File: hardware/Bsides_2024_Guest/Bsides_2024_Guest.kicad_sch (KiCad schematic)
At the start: 44 parts, among them J1 Add_On, J2 Battery, J3 Battery, J4 OLED, J5 Conn_01x05, J6 Conn_01x05, P1 USB_C_Plug_USB2.0, Q1 DMG3415U-7, SW1 ON, SW2 RESET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

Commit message: feat(Hw): Update schematics
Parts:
- J4: manf# I2C SH1106 Display Oled Azul 128×64 1.3 ” -> Display OLED 128×32 0.91 I2C SSD1306 Blanco / Azul
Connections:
- net GND: now also J4.4 (Pin_4); no longer J4.2 (Pin_2)
- net SCL: now also J4.2 (Pin_2); no longer J4.3 (Pin_3)
- net SDA: now also J4.1 (Pin_1); no longer J4.4 (Pin_4)
- net VOUT: now also J4.3 (Pin_3); no longer J4.1 (Pin_1)
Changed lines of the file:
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@@
 	(wire
 		(pts
-			(xy 76.2 118.11) (xy 82.55 118.11)
-		)
-		(stroke
-			(width 0)
-			(type default)
-		)
-	)
-	(wire
-		(pts
 			(xy 192.024 119.761) (xy 196.215 119.761)
 		)
@@
 	(wire
 		(pts
-			(xy 76.2 120.65) (xy 82.55 120.65)
-		)
-		(stroke
-			(width 0)
-			(type default)
-		)
-	)
-	(wire
-		(pts
 			(xy 199.136 69.85) (xy 199.136 70.358)
 		)
@@
 	(wire
 		(pts
+			(xy 80.01 116.84) (xy 77.47 116.84)
+		)
+		(stroke
+			(width 0)
+			(type default)
+		)
+	)
+	(wire
+		(pts
 			(xy 58.674 79.756) (xy 62.484 79.756)
 		)
@@
 	(wire
 		(pts
-			(xy 76.2 123.19) (xy 82.55 123.19)
-		)
-		(stroke
-			(width 0)
-			(type default)
-		)
-	)
-	(wire
-		(pts
 			(xy 58.674 37.846) (xy 70.612 37.846)
 		)
@@
 	(wire
 		(pts
+			(xy 80.01 119.38) (xy 77.47 119.38)
+		)
+		(stroke
+			(width 0)
+			(type default)
+		)
+	)
+	(wire
+		(pts
 			(xy 262.89 119.761) (xy 266.7 119.761)
 		)
@@
 	(wire
 		(pts
-			(xy 76.2 115.57) (xy 82.55 115.57)
-		)
-		(stroke
-			(width 0)
-			(type default)
-		)
-	)
-	(wire
-		(pts
 			(xy 26.67 116.84) (xy 29.21 116.84)
 		)
@@
 	(wire
 		(pts
+			(xy 80.01 121.92) (xy 77.47 121.92)
+		)
+		(stroke
+			(width 0)
+			(type default)
+		)
+	)
+	(wire
+		(pts
 			(xy 251.587 89.154) (xy 251.587 85.598)
 		)
@@
 	(wire
 		(pts
+			(xy 80.01 124.46) (xy 77.47 124.46)
+		)
+		(stroke
+			(width 0)
+			(type default)
+		)
+	)
+	(wire
+		(pts
 			(xy 237.49 119.761) (xy 241.808 119.761)
 		)
@@
 		)
 	)
-	(label "SDA"
-		(at 76.2 123.19 0)
-		(fields_autoplaced yes)
-		(effects
-			(font
-				(size 1.27 1.27)
-			)
-			(justify left bottom)
-		)
-	)
 	(label "VOUT"
 		(at 213.36 118.11 0)
@@
 		)
 	)
-	(label "SCL"
-		(at 76.2 120.65 0)
-		(fields_autoplaced yes)
-		(effects
-			(font
-				(size 1.27 1.27)
-			)
-			(justify left bottom)
-		)
-	)
 	(label "PIN"
 		(at 172.466 131.826 0)
@@
 		)
 	)
-	(label "GND"
-		(at 76.2 118.11 0)
+	(label "D+"
+		(at 149.606 59.69 0)
 		(fields_autoplaced yes)
 		(effects
@@
 		)
 	)
-	(label "D+"
-		(at 149.606 59.69 0)
+	(label "D-"
+		(at 29.972 65.786 0)
 		(fields_autoplaced yes)
 		(effects
@@
 		)
 	)
-	(label "D-"
-		(at 29.972 65.786 0)
+	(label "SCL"
+		(at 77.47 119.38 180)
 		(fields_autoplaced yes)
 		(effects
@@
 				(size 1.27 1.27)
 			)
-			(justify left bottom)
+			(justify right bottom)
 		)
 	)
@@
 		)
 	)
+	(label "GND"
+		(at 77.47 124.46 180)
+		(fields_autoplaced yes)
+		(effects
+			(font
+				(size 1.27 1.27)
+			)
+			(justify right bottom)
+		)
+	)
 	(label "BOOT"
 		(at 182.753 67.818 180)
@@
 		)
 	)
-	(label "VOUT"
-		(at 76.2 115.57 0)
-		(fields_autoplaced yes)
-		(effects
-			(font
-				(size 1.27 1.27)
-			)
-			(justify left bottom)
-		)
-	)
 	(label "GPIO15"
 		(at 62.484 71.374 0)
@@
 		)
 	)
+	(label "SDA"
+		(at 77.47 116.84 180)
+		(fields_autoplaced yes)
+		(effects
+			(font
+				(size 1.27 1.27)
+			)
+			(justify right bottom)
+		)
+	)
 	(label "VOUT"
 		(at 85.09 58.42 0)
@@
 		)
 	)
+	(label "VOUT"
+		(at 77.47 121.92 180)
+		(fields_autoplaced yes)
+		(effects
+			(font
+				(size 1.27 1.27)
+			)
+			(justify right bottom)
+		)
+	)
 	(label "BOOT"
 		(at 24.638 71.374 0)
@@
 	)
 	(symbol
+		(lib_id "Connector:Screw_Terminal_01x04")
+		(at 85.09 119.38 0)
+		(unit 1)
+		(exclude_from_sim no)
+		(in_bom yes)
+		(on_board yes)
+		(dnp no)
+		(fields_autoplaced yes)
+		(property "Reference" "J4"
+			(at 87.376 119.3799 0)
+			(effects
+				(font
+					(size 1.27 1.27)
+				)
+				(justify left)
+			)
+		)
+		(property "Value" "OLED"
+			(at 87.376 121.9199 0)
+			(effects
+				(font
+					(size 1.27 1.27)
+				)
+				(justify left)
+			)
+		)
+		(property "Footprint" "bsides:Display OLED 128 x32"
+			(at 85.09 119.38 0)
+			(effects
+				(font
+					(size 1.27 1.27)
+				)
+				(hide yes)
+			)
+		)
+		(property "Datasheet" ""
+			(at 85.09 119.38 0)
+			(effects
+				(font
+					(size 1.27 1.27)
+				)
+				(hide yes)
+			)
+		)
+		(property "Description" ""
+			(at 85.09 119.38 0)
+			(effects
+				(font
+					(size 1.27 1.27)
+				)
+				(hide yes)
+			)
+		)
+		(property "manf#" "Display OLED 128×32 0.91 I2C SSD1306 Blanco / Azul"
+			(at 85.09 119.38 0)
+			(effects
+				(font
+					(size 1.27 1.27)
+				)
+				(hide yes)
+			)
+		)
+		(property "provedor" "UNIT Electronics"
+			(at 85.09 119.38 0)
+			(effects
+				(font
+					(size 1.27 1.27)
+				)
+				(hide yes)
+			)
+		)
+		(pin "1"
+		)
+		(pin "2"
+		)
+		(pin "3"
+		)
+		(pin "4"
+		)
+		(instances
+			(project "Bsides_2024_Guest"
+				(path "/21a57a81-777f-4f81-b806-a7171bf6ef6c"
+					(reference "J4")
+					(unit 1)
+				)
+			)
+		)
+	)
+	(symbol
 		(lib_id "power:GND")
 		(at 199.39 55.88 0)
@@
 					(unit 1)
 				)
-			)
-		)
-	)
-	(symbol
-		(lib_id "Connector:Screw_Terminal_01x04")
-		(at 87.63 118.11 0)
-		(unit 1)
-		(exclude_from_sim no)
-		(in_bom yes)
-		(on_board yes)
-		(dnp no)
-		(fields_autoplaced yes)
-		(property "Reference" "J4"
-			(at 89.916 118.1099 0)
-			(effects
-				(font
-					(size 1.27 1.27)
-				)
-				(justify left)
-			)
-		)
-		(property "Value" "OLED"
-			(at 89.916 120.6499 0)
-			(effects
-				(font
-					(size 1.27 1.27)
-				)
-				(justify left)
-			)
-		)
-		(property "Footprint" "bsides:Display OLED 128 x32"
-			(at 87.63 118.11 0)
-			(effects
-				(font
-					(size 1.27 1.27)
-				)
-				(hide yes)
-			)
-		)
-		(property "Datasheet" "~"
-			(at 87.63 118.11 0)
-			(effects
-				(font
-					(size 1.27 1.27)
-				)
-				(hide yes)
-			)
-		)
-		(property "Description" ""
-			(at 87.63 118.11 0)
-			(effects
-				(font
-					(size 1.27 1.27)
-				)
-				(hide yes)
-			)
-		)
-		(property "manf#" "I2C SH1106 Display Oled Azul 128×64 1.3 ” "
-			(at 87.63 118.11 0)
-			(effects
-				(font
-					(size 1.27 1.27)
-				)
-				(hide yes)
-			)
-		)
-		(property "provedor" "UNIT Electronics"
-			(at 87.63 118.11 0)
-			(effects
-				(font
-					(size 1.27 1.27)
-				)
-				(hide yes)
-			)
-		)
-		(pin "1"
-		)
-		(pin "2"
-		)
-		(pin "3"
-		)
-		(pin "4"
-		)
-		(instances
-			(project "Bsides_2024_Guest"
-				(path "/21a57a81-777f-4f81-b806-a7171bf6ef6c"
-					(reference "J4")
-					(unit 1)
-				)

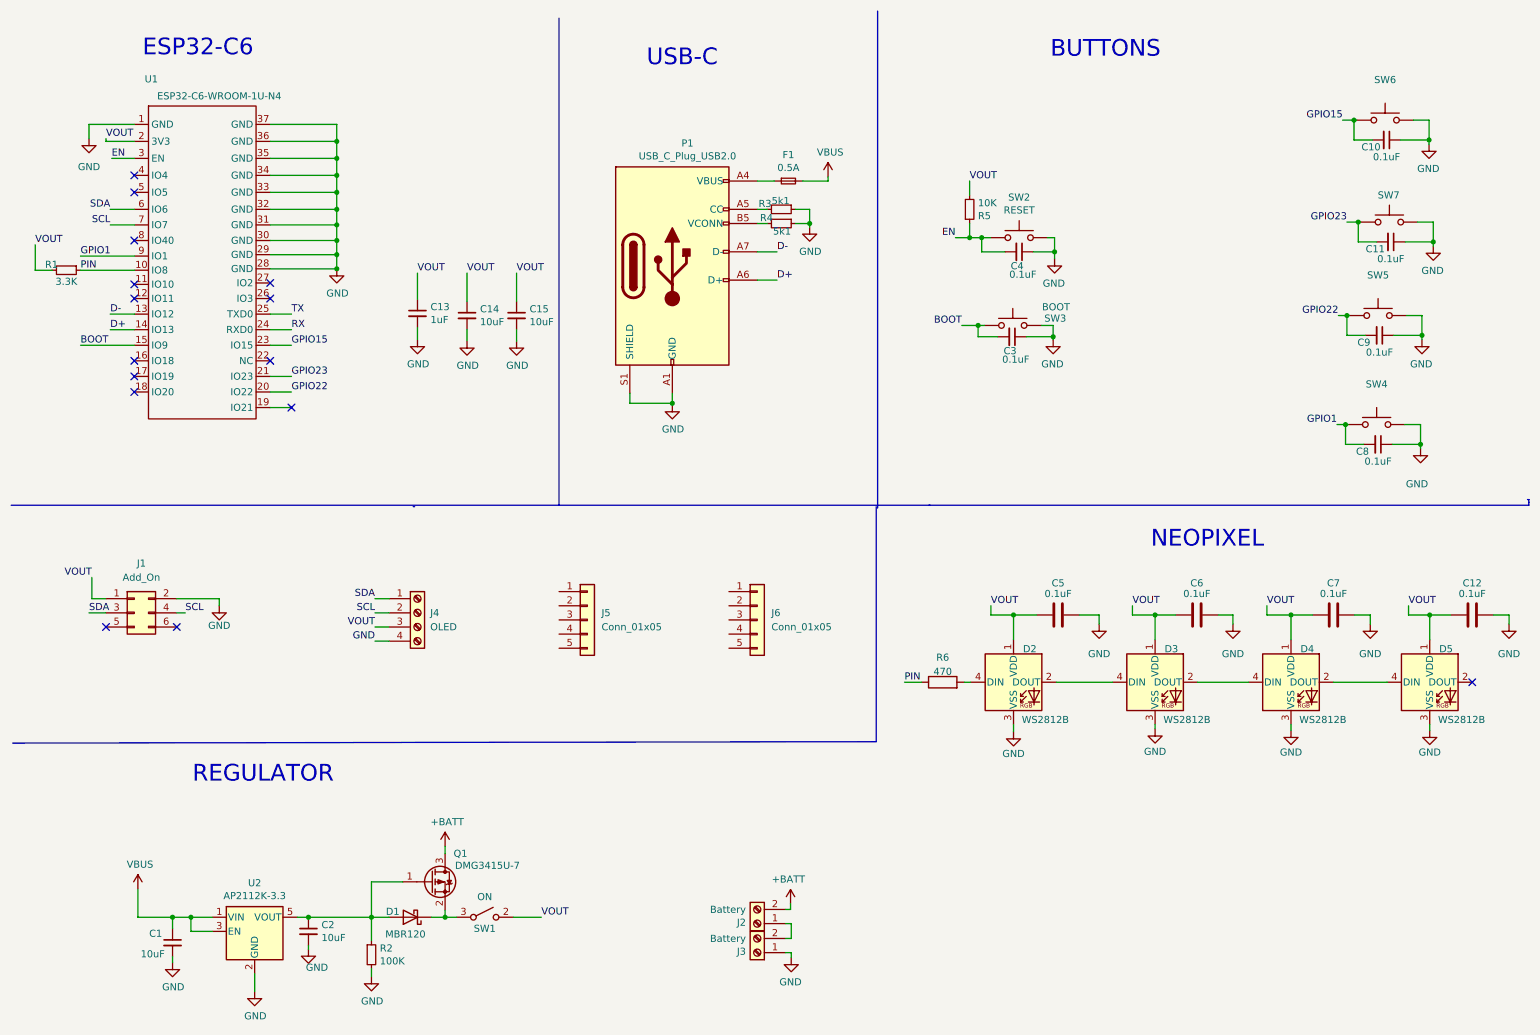
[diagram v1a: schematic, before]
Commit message: feat(Hw): Update route
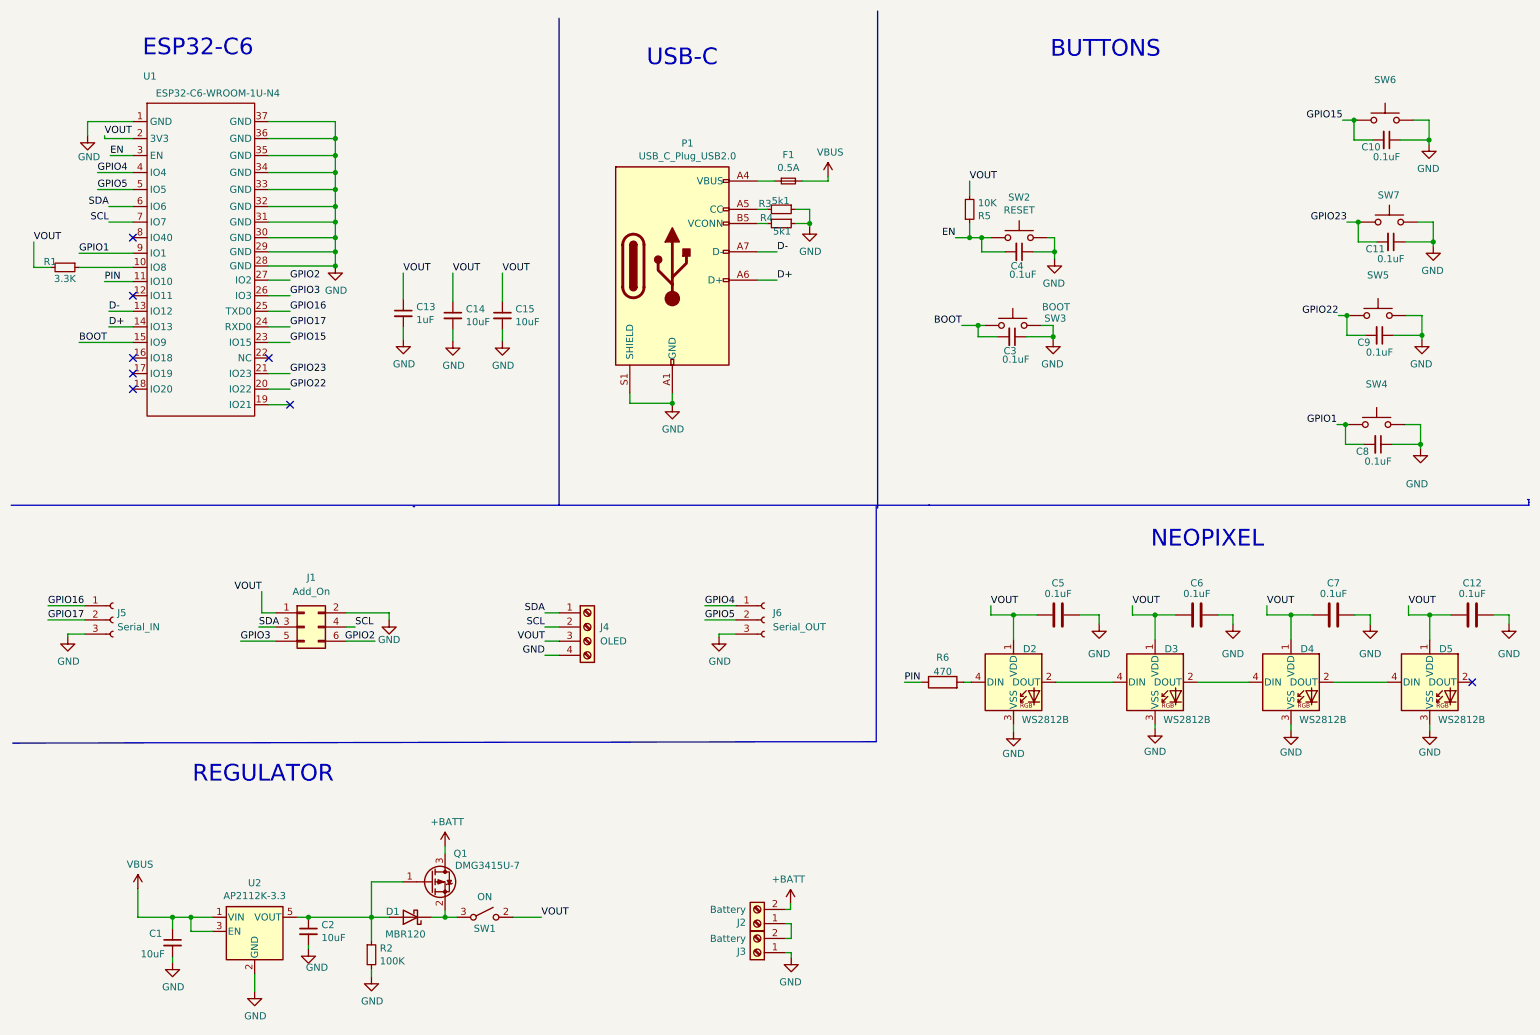
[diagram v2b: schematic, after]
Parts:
- removed J5, J6: Conn_01x05, Connector_PinHeader_2.54mm:PinHeader_1x05_P2.54mm_Vertical, symbol Connector_Generic:Conn_01x05
- added J5: Serial_IN, Connector_PinHeader_2.54mm:PinHeader_1x03_P2.54mm_Vertical, symbol Connector:Conn_01x03_Socket
- added J6: Serial_OUT, Connector_PinSocket_2.54mm:PinSocket_1x03_P2.54mm_Vertical, symbol Connector:Conn_01x03_Socket
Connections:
- net GND: now also J5.3 (Pin_3), J6.3 (Pin_3)
- net PIN: now also U1.11 (IO10); no longer R1.1, U1.10 (IO8)
- net GPIO3: now reaches U1.26 (IO3)
- net GPIO3: now also J1.5 (Pin_5)
- net GPIO2: now reaches U1.27 (IO2)
- net GPIO2: now also J1.6 (Pin_6)
- net GPIO4: now reaches U1.4 (IO4)
- net GPIO4: now also J6.1 (Pin_1)
- net GPIO5: now reaches U1.5 (IO5)
- net GPIO5: now also J6.2 (Pin_2)
- net RX renamed GPIO17
- net GPIO17: now also J5.2 (Pin_2)
- net TX renamed GPIO16
- net GPIO16: now also J5.1 (Pin_1)
- new net: R1.1, U1.10 (IO8)
- no-connect marks 15 -> 8
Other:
- moved on the sheet: C13, C14, C15, J1, J4, R1, U1

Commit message: Update route and schematic
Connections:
- net GPIO1 renamed LEFT
- net LEFT: now also SW7.2; no longer SW4.2
- net GPIO15 renamed RIGHT
- net GPIO22 renamed UP
- net UP: now also SW4.2; no longer SW5.2
- net GPIO23 renamed DOWN
- net DOWN: now also SW5.2; no longer SW7.2
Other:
- moved on the sheet: C8, C9, SW4, SW5, SW7

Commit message: Feat(Hw): Update PCB
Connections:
- net DOWN: now also C9.2; no longer C11.2
- net LEFT: now also C10.2, SW6.2; no longer C8.2, SW7.2
- net RIGHT: now also C11.2, SW7.2; no longer C10.2, SW6.2
- net UP: now also C8.2; no longer C9.2
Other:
- moved on the sheet: C10, SW4, SW5, SW6, SW7
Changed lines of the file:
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@@
 	)
 	(junction
-		(at 266.573 34.544)
+		(at 266.954 32.766)
 		(diameter 0)
 		(color 0 0 0 0)
@@
 	)
 	(junction
-		(at 253.111 30.988)
+		(at 253.492 29.21)
 		(diameter 0)
 		(color 0 0 0 0)
@@
 	(wire
 		(pts
-			(xy 252.222 85.09) (xy 250.698 85.09)
-		)
-		(stroke
-			(width 0)
-			(type default)
-		)
-	)
-	(wire
-		(pts
 			(xy 175.514 131.826) (xy 172.466 131.826)
 		)
@@
 	(wire
 		(pts
-			(xy 266.573 34.544) (xy 266.573 35.306)
+			(xy 266.954 32.766) (xy 266.954 33.528)
 		)
 		(stroke
@@
 	(wire
 		(pts
-			(xy 266.573 34.544) (xy 261.493 34.544)
+			(xy 266.954 32.766) (xy 261.874 32.766)
 		)
 		(stroke
@@
 	(wire
 		(pts
-			(xy 266.573 30.988) (xy 266.573 34.544)
+			(xy 266.954 29.21) (xy 266.954 32.766)
 		)
 		(stroke
@@
 	(wire
 		(pts
-			(xy 256.413 34.544) (xy 253.111 34.544)
+			(xy 256.794 32.766) (xy 253.492 32.766)
 		)
 		(stroke
@@
 	(wire
 		(pts
-			(xy 253.111 34.544) (xy 253.111 30.988)
+			(xy 253.492 32.766) (xy 253.492 29.21)
 		)
 		(stroke
@@
 	(wire
 		(pts
-			(xy 263.779 30.988) (xy 266.573 30.988)
+			(xy 264.16 29.21) (xy 266.954 29.21)
 		)
 		(stroke
@@
 	(wire
 		(pts
-			(xy 253.111 30.988) (xy 251.079 30.988)
+			(xy 253.492 29.21) (xy 251.46 29.21)
 		)
 		(stroke
@@
 	(wire
 		(pts
-			(xy 253.619 30.988) (xy 253.111 30.988)
+			(xy 254 29.21) (xy 253.492 29.21)
 		)
 		(stroke
@@
 	(wire
 		(pts
-			(xy 253.492 66.04) (xy 251.968 66.04)
+			(xy 253.492 66.04) (xy 251.46 66.04)
 		)
 		(stroke
@@
 	(wire
 		(pts
+			(xy 250.19 85.09) (xy 252.222 85.09)
+		)
+		(stroke
+			(width 0)
+			(type default)
+		)
+	)
+	(wire
+		(pts
 			(xy 34.036 37.338) (xy 29.972 37.338)
 		)
@@
 	)
 	(label "UP"
-		(at 251.968 66.04 180)
+		(at 250.19 85.09 180)
 		(fields_autoplaced yes)
 		(effects
@@
 	)
 	(label "LEFT"
-		(at 250.698 85.09 180)
+		(at 251.46 29.21 180)
 		(fields_autoplaced yes)
 		(effects
@@
 	)
 	(label "DOWN"
-		(at 251.46 49.53 180)
+		(at 251.46 66.04 180)
 		(fields_autoplaced yes)
 		(effects
@@
 	)
 	(label "RIGHT"
-		(at 251.079 30.988 180)
+		(at 251.46 49.53 180)
 		(fields_autoplaced yes)
 		(effects
@@
 	(symbol
 		(lib_id "Switch:SW_Push")
-		(at 259.08 49.53 0)
+		(at 259.08 66.04 0)
 		(mirror y)
 		(unit 1)
@@
 		(dnp no)
 		(property "Reference" "SW5"
-			(at 259.08 42.291 0)
+			(at 259.08 58.801 0)
 			(effects
 				(font
@@
 		)
 		(property "Value" "~"
-			(at 259.08 44.6024 0)
+			(at 259.08 61.1124 0)
 			(effects
 				(font
@@
 		)
 		(property "Footprint" "Button_Switch_SMD:SW_SPST_TL3342"
-			(at 259.08 44.45 0)
+			(at 259.08 60.96 0)
 			(effects
 				(font
@@
 		)
 		(property "Datasheet" "https://datasheet.lcsc.com/lcsc/2205161616_E-Switch-TL3342F450QG_C2886897.pdf"
-			(at 259.08 44.45 0)
+			(at 259.08 60.96 0)
 			(effects
 				(font
@@
 		)
 		(property "Description" ""
-			(at 259.08 49.53 0)
+			(at 259.08 66.04 0)
 			(effects
 				(font
@@
 		)
 		(property "manf#" ""
-			(at 259.08 49.53 0)
+			(at 259.08 66.04 0)
 			(effects
 				(font
@@
 		)
 		(property "LCSC#" "C2886897"
-			(at 259.08 49.53 0)
+			(at 259.08 66.04 0)
 			(effects
 				(font
@@
 		)
 		(property "provedor" "LCSC"
-			(at 259.08 49.53 0)
+			(at 259.08 66.04 0)
 			(effects
 				(font
@@
 	(symbol
 		(lib_id "Switch:SW_Push")
-		(at 257.81 85.09 0)
+		(at 259.08 49.53 0)
 		(mirror y)
 		(unit 1)
@@
 		(dnp no)
 		(property "Reference" "SW7"
-			(at 257.683 80.264 0)
+			(at 258.953 44.704 0)
 			(effects
 				(font
@@
 		)
 		(property "Value" "~"
-			(at 257.81 80.1624 0)
+			(at 259.08 44.6024 0)
 			(effects
 				(font
@@
 		)
 		(property "Footprint" "Button_Switch_SMD:SW_SPST_TL3342"
-			(at 257.81 80.01 0)
+			(at 259.08 44.45 0)
 			(effects
 				(font
@@
 		)
 		(property "Datasheet" "https://datasheet.lcsc.com/lcsc/2205161616_E-Switch-TL3342F450QG_C2886897.pdf"
-			(at 257.81 80.01 0)
+			(at 259.08 44.45 0)
 			(effects
 				(font
@@
 		)
 		(property "Description" ""
-			(at 257.81 85.09 0)
+			(at 259.08 49.53 0)
 			(effects
 				(font
@@
 		)
 		(property "manf#" ""
-			(at 257.81 85.09 0)
+			(at 259.08 49.53 0)
 			(effects
 				(font
@@
 		)
 		(property "LCSC#" "C2886897"
-			(at 257.81 85.09 0)
+			(at 259.08 49.53 0)
 			(effects
 				(font
@@
 		)
 		(property "provedor" "LCSC"
-			(at 257.81 85.09 0)
+			(at 259.08 49.53 0)
 			(effects
 				(font
@@
 	(symbol
 		(lib_id "Switch:SW_Push")
-		(at 258.699 30.988 0)
+		(at 259.08 29.21 0)
 		(mirror y)
 		(unit 1)
@@
 		(dnp no)
 		(property "Reference" "SW6"
-			(at 258.699 23.749 0)
+			(at 259.08 21.971 0)
 			(effects
 				(font
@@
 		)
 		(property "Value" "RESET"
-			(at 258.699 26.0604 0)
+			(at 259.08 24.2824 0)
 			(effects
 				(font
@@
 		)
 		(property "Footprint" "Button_Switch_SMD:SW_SPST_TL3342"
-			(at 258.699 25.908 0)
+			(at 259.08 24.13 0)
 			(effects
 				(font
@@
 		)
 		(property "Datasheet" "https://datasheet.lcsc.com/lcsc/2205161616_E-Switch-TL3342F450QG_C2886897.pdf"
-			(at 258.699 25.908 0)
+			(at 259.08 24.13 0)
 			(effects
 				(font
@@
 		)
 		(property "Description" ""
-			(at 258.699 30.988 0)
+			(at 259.08 29.21 0)
 			(effects
 				(font
@@
 		)
 		(property "manf#" ""
-			(at 258.699 30.988 0)
+			(at 259.08 29.21 0)
 			(effects
 				(font
@@
 		)
 		(property "LCSC#" "C2886897"
-			(at 258.699 30.988 0)
+			(at 259.08 29.21 0)
 			(effects
 				(font
@@
 		)
 		(property "provedor" "LCSC"
-			(at 258.699 30.988 0)
+			(at 259.08 29.21 0)
 			(effects
 				(font
@@
 	(symbol
 		(lib_id "Switch:SW_Push")
-		(at 259.08 66.04 0)
+		(at 257.81 85.09 0)
 		(mirror y)
 		(unit 1)
@@
 		(dnp no)
 		(property "Reference" "SW4"
-			(at 259.08 58.801 0)
+			(at 257.81 77.851 0)
 			(effects
 				(font
@@
 		)
 		(property "Value" "RESET"
-			(at 259.08 61.1124 0)
+			(at 257.81 80.1624 0)
 			(effects
 				(font
@@
 		)
 		(property "Footprint" "Button_Switch_SMD:SW_SPST_TL3342"
-			(at 259.08 60.96 0)
+			(at 257.81 80.01 0)
 			(effects
 				(font
@@
 		)
 		(property "Datasheet" "https://datasheet.lcsc.com/lcsc/2205161616_E-Switch-TL3342F450QG_C2886897.pdf"
-			(at 259.08 60.96 0)
+			(at 257.81 80.01 0)
 			(effects
 				(font
@@
 		)
 		(property "Description" ""
-			(at 259.08 66.04 0)
+			(at 257.81 85.09 0)
 			(effects
 				(font
@@
 		)
 		(property "manf#" ""
-			(at 259.08 66.04 0)
+			(at 257.81 85.09 0)
 			(effects
 				(font
@@
 		)
 		(property "LCSC#" "C2886897"
-			(at 259.08 66.04 0)
+			(at 257.81 85.09 0)
 			(effects
 				(font
@@
 		)
 		(property "provedor" "LCSC"
-			(at 259.08 66.04 0)
+			(at 257.81 85.09 0)
 			(effects
 				(font
@@
 	(symbol
 		(lib_id "Device:C_Small")
-		(at 258.953 34.544 270)
+		(at 259.334 32.766 270)
 		(mirror x)
 		(unit 1)
@@
 		(dnp no)
 		(property "Reference" "C10"
-			(at 256.159 35.814 90)
+			(at 256.54 34.036 90)
 			(effects
 				(font
@@
 		)
 		(property "Value" "0.1uF"
-			(at 258.953 37.592 90)
+			(at 259.334 35.814 90)
 			(effects
 				(font
@@
 		)
 		(property "Footprint" "Capacitor_SMD:C_0603_1608Metric"
-			(at 258.953 34.544 0)
+			(at 259.334 32.766 0)
 			(effects
 				(font
@@
 		)
 		(property "Datasheet" "~"
-			(at 258.953 34.544 0)
+			(at 259.334 32.766 0)
 			(effects
 				(font
@@
 		)
 		(property "Description" "Unpolarized capacitor, small symbol"
-			(at 258.953 34.544 0)
+			(at 259.334 32.766 0)
 			(effects
 				(font
@@
 	(symbol
 		(lib_id "power:GND")
-		(at 266.573 35.306 0)
+		(at 266.954 33.528 0)
 		(mirror y)
 		(unit 1)
@@
 		(dnp no)
 		(property "Reference" "#PWR033"
-			(at 266.573 41.656 0)
+			(at 266.954 39.878 0)
 			(effects
 				(font
@@
 		)
 		(property "Value" "GND"
-			(at 266.446 39.7002 0)
+			(at 266.827 37.9222 0)
 			(effects
 				(font
@@
 		)
 		(property "Footprint" ""
-			(at 266.573 35.306 0)
+			(at 266.954 33.528 0)
 			(effects
 				(font
@@
 		)
 		(property "Datasheet" ""
-			(at 266.573 35.306 0)
+			(at 266.954 33.528 0)
 			(effects
 				(font
@@
 		)
 		(property "Description" ""
-			(at 266.573 35.306 0)
+			(at 266.954 33.528 0)
 			(effects
 				(font
